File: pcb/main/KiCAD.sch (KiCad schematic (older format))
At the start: 368 parts, among them Q1 2N7002, SW1 CherryMX, SW10 CherryMX, SW11 CherryMX, SW12 CherryMX, SW13 CherryMX, SW14 CherryMX, SW15 CherryMX, SW16 CherryMX, SW17 CherryMX, SW18 CherryMX, SW19 CherryMX, SW2 CherryMX, SW20 CherryMX, SW21 CherryMX, SW22 CherryMX, SW23 CherryMX, SW24 CherryMX, SW25 CherryMX, SW26 CherryMX, SW27 CherryMX, SW28 CherryMX, SW29 CherryMX, SW3 CherryMX, SW30 CherryMX, SW31 CherryMX, SW32 CherryMX, SW33 CherryMX, SW34 CherryMX, SW35 CherryMX, SW36 CherryMX, SW37 CherryMX, SW38 CherryMX, SW39 CherryMX, SW4 CherryMX, SW40 CherryMX, SW41 CherryMX, SW42 CherryMX, SW43 CherryMX, SW44 CherryMX, SW45 CherryMX, SW46 CherryMX, SW47 CherryMX, SW48 CherryMX, SW49 CherryMX, SW5 CherryMX, SW50 CherryMX, SW51 CherryMX, SW52 CherryMX, SW53 CherryMX, SW54 CherryMX, SW55 CherryMX, SW56 CherryMX, SW57 CherryMX, SW58 CherryMX, SW59 CherryMX, SW6 CherryMX, SW60 CherryMX, SW61 CherryMX, SW62 CherryMX, SW63 CherryMX, SW64 CherryMX, SW65 CherryMX, SW66 CherryMX, SW67 CherryMX, SW68 CherryMX, SW69 CherryMX, SW7 CherryMX, SW70 CherryMX, SW71 CherryMX, SW72 CherryMX, SW73 CherryMX, SW74 CherryMX, SW75 CherryMX, SW76 CherryMX, SW77 CherryMX, SW78 CherryMX, SW79 CherryMX, SW8 CherryMX, SW80 CherryMX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

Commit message: Add files via upload
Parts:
- removed U1: Pico, RPi_Pico:RPi_Pico_SMD_TH, symbol KiCAD-rescue:Pico-RaspberryPi_Pico
- added U?: Pico, RPi_Pico:RPi_Pico_SMD_TH, symbol RaspberryPi_Pico:Pico
- C1: footprint (none) -> Capacitor_SMD:C_0603_1608Metric
- R89: footprint (none) -> Resistor_SMD:R_0603_1608Metric
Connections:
- net Col0: now also U?.1 (GPIO0)
- net Col1: now also U?.9 (GPIO6)
- net Col2: now also U?.4 (GPIO2)
- net Col3: now also U?.2 (GPIO1)
- net Col4: now also U?.14 (GPIO10)
- net Col5: now also U?.12 (GPIO9)
- net Col6: now also U?.11 (GPIO8)
- net Col7: now also U?.10 (GPIO7)
- net Col8: now also U?.7 (GPIO5)
- net Col9: now also U?.6 (GPIO4)
- net GND: now also U?.13 (GND), U?.18 (GND), U?.23 (GND), U?.28 (GND), U?.3 (GND), U?.33 (AGND), U?.38 (GND), U?.8 (GND)
- net PWM: now also U?.29 (GPIO22)
- net Row0: now also U?.5 (GPIO3)
- net Row1: now also U?.15 (GPIO11)
- net Row2: now also U?.17 (GPIO13)
- net Row3: now also U?.16 (GPIO12)
- net Row4: now also U?.19 (GPIO14)
- net Row5: now also U?.20 (GPIO15)
- net Row6: now also U?.27 (GPIO21)
- net Row7: now also U?.26 (GPIO20)
- net Row8: now also U?.25 (GPIO19)
- net Row9: now also U?.24 (GPIO18)
- net VBUS: now also U?.40 (VBUS)
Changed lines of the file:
@@
-$EndComp
-$Comp
-L KiCAD-rescue:Pico-RaspberryPi_Pico U1
-U 1 1 63A3E8CA
-P 2250 7850
-F 0 "U1" H 2250 9065 50  0000 C CNN
-F 1 "Pico" H 2250 8974 50  0000 C CNN
-F 2 "RPi_Pico:RPi_Pico_SMD_TH" V 2250 7850 50  0001 C CNN
-F 3 "" H 2250 7850 50  0001 C CNN
-	1    2250 7850
-	1    0    0    -1
 $EndComp
 $Comp
@@
 F 0 "C1" H 3565 7046 50  0000 L CNN
 F 1 "3.3u" H 3565 6955 50  0000 L CNN
-F 2 "" H 3488 6850 50  0001 C CNN
+F 2 "Capacitor_SMD:C_0603_1608Metric" H 3488 6850 50  0001 C CNN
 F 3 "~" H 3450 7000 50  0001 C CNN
 	1    3450 7000
@@
 F 0 "R89" H 2120 5296 50  0000 L CNN
 F 1 "10k" H 2120 5205 50  0000 L CNN
-F 2 "" V 1980 5250 50  0001 C CNN
+F 2 "Resistor_SMD:R_0603_1608Metric" V 1980 5250 50  0001 C CNN
 F 3 "~" H 2050 5250 50  0001 C CNN
 	1    2050 5250
@@
 Wire Wire Line
 	3450 7300 3450 7400
+$Comp
+L RaspberryPi_Pico:Pico U?
+U 1 1 61447957
+P 2250 7850
+F 0 "U?" H 2250 9065 50  0000 C CNN
+F 1 "Pico" H 2250 8974 50  0000 C CNN
+F 2 "RPi_Pico:RPi_Pico_SMD_TH" V 2250 7850 50  0001 C CNN
+F 3 "" H 2250 7850 50  0001 C CNN
+	1    2250 7850
+	1    0    0    -1
+$EndComp
 $EndSCHEMATC

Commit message: 復元した
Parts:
- removed U?: Pico, RPi_Pico:RPi_Pico_SMD_TH, symbol RaspberryPi_Pico:Pico
- added U?: Pico, RPi_Pico:RPi_Pico_SMD_TH, symbol RaspberryPi_Pico:Pico
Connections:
- net Col0: now also U?.1 (GPIO0)
- net Col1: now also U?.9 (GPIO6)
- net Col2: now also U?.4 (GPIO2)
- net Col3: now also U?.2 (GPIO1)
- net Col4: now also U?.14 (GPIO10)
- net Col5: now also U?.12 (GPIO9)
- net Col6: now also U?.11 (GPIO8)
- net Col7: now also U?.10 (GPIO7)
- net Col8: now also U?.7 (GPIO5)
- net Col9: now also U?.6 (GPIO4)
- net GND: now also U?.13 (GND), U?.18 (GND), U?.23 (GND), U?.28 (GND), U?.3 (GND), U?.33 (AGND), U?.38 (GND), U?.8 (GND)
- net PWM: now also U?.29 (GPIO22)
- net Row0: now also U?.5 (GPIO3)
- net Row1: now also U?.15 (GPIO11)
- net Row2: now also U?.17 (GPIO13)
- net Row3: now also U?.16 (GPIO12)
- net Row4: now also U?.19 (GPIO14)
- net Row5: now also U?.20 (GPIO15)
- net Row6: now also U?.27 (GPIO21)
- net Row7: now also U?.26 (GPIO20)
- net Row8: now also U?.25 (GPIO19)
- net Row9: now also U?.24 (GPIO18)
- net VBUS: now also U?.40 (VBUS)
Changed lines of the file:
@@
 $Comp
 L RaspberryPi_Pico:Pico U?
-U 1 1 61447957
+U 1 1 6143F7AA
 P 2250 7850
 F 0 "U?" H 2250 9065 50  0000 C CNN

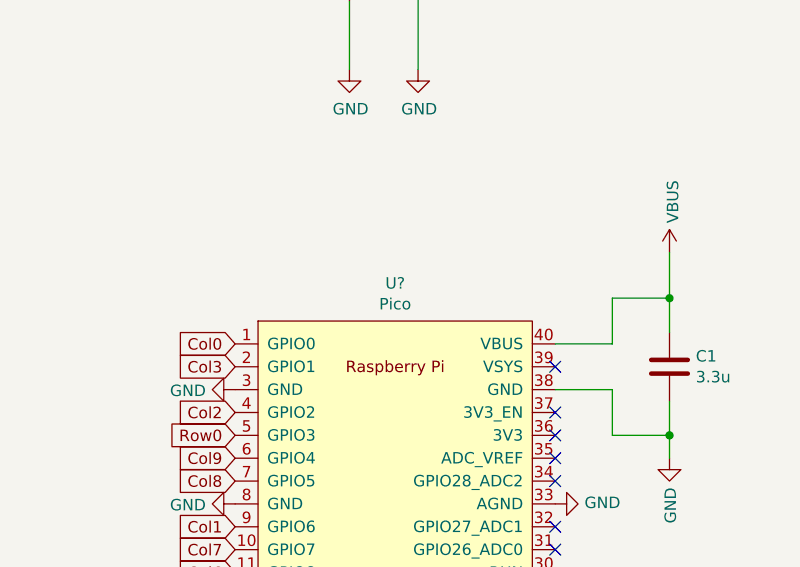
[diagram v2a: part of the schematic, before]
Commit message: step ファイルの追加
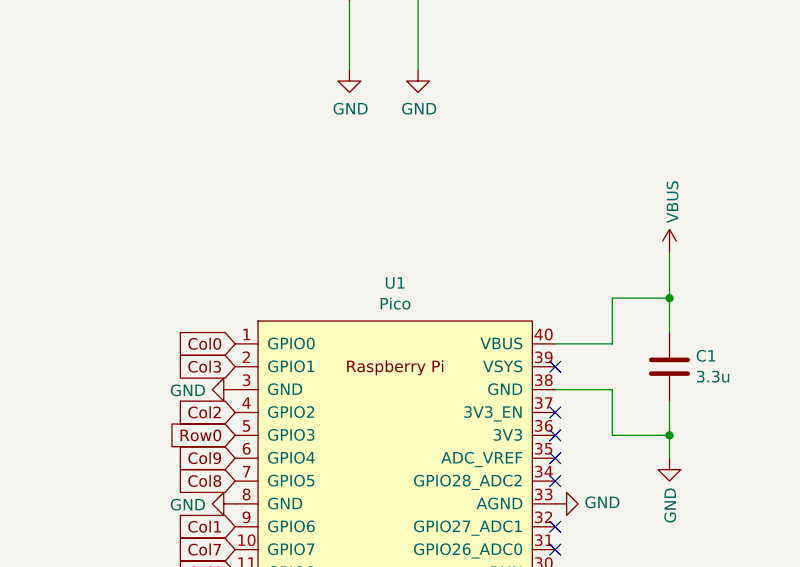
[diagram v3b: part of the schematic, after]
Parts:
- gave numbers to parts that had none: 1
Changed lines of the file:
@@
 	3450 7300 3450 7400
 $Comp
-L RaspberryPi_Pico:Pico U?
+L RaspberryPi_Pico:Pico U1
 U 1 1 6143F7AA
 P 2250 7850
-F 0 "U?" H 2250 9065 50  0000 C CNN
+F 0 "U1" H 2250 9065 50  0000 C CNN
 F 1 "Pico" H 2250 8974 50  0000 C CNN
 F 2 "RPi_Pico:RPi_Pico_SMD_TH" V 2250 7850 50  0001 C CNN
